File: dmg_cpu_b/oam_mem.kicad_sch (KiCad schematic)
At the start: 27 parts

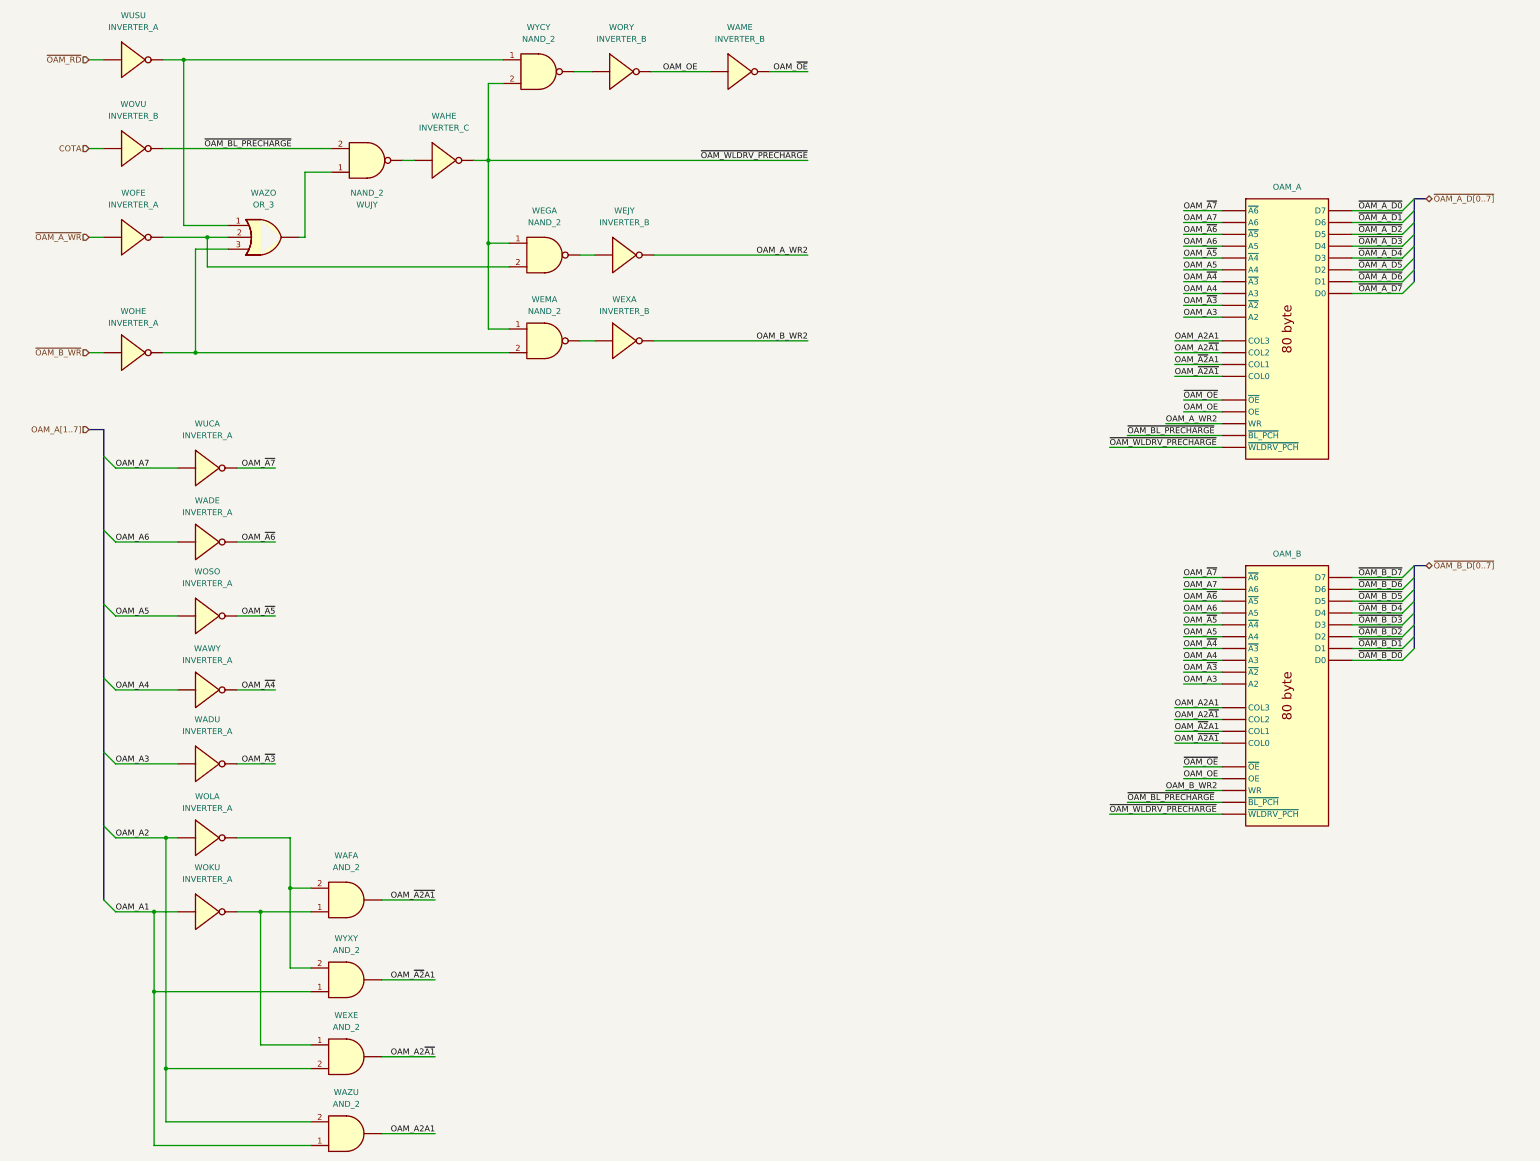
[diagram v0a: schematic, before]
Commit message: Give more meaningful names to cell types
Before this commit, many of the cells types in the chip were named in a
sloppy manner. The different inverter, latch and flip flop valiants were
just suffixed with A, B, C, D, ... Those suffixes gave no information
about the actual differences. They had to be looked up in the
documentation. Now the names of cell types with different variants have
changed:

* Inverter types are named NOT_X1, NOT_X2, NOT_X3, ... The _Xn suffix
  reflects the drive strength of the cell. X1 is the drive strength of
  the weakest inverter, X2 is double the drive strength of the weakest
  inverter.
* Flip flop types are named DFFR, DFFR_CC, DFFR_CC_Q. DFFR is a normal
  data flip flop with reset and a single clock input. The suffix _CC is
  added to flip flops that have two complementary clock inputs (CLK and
  /CLK). Flip flops that only have the positive Q output are suffixed
  with _Q.
* Latch types are named similar to flip flops: DLATCH, DLATCH_EE,
  DLATCH_EE_Q. The suffix _EE is given to latches that require
  "externally inverted enable" signals (ENA and /ENA).
* I/O pad types all start with PAD_BIDIR, PAD_IN or PAD_OUT. They also
  have suffixes that describe what makes them unique, like _PU for
  pull-ups.

Other minor changes were made to align the names with common naming
schemes of other cell libraries.
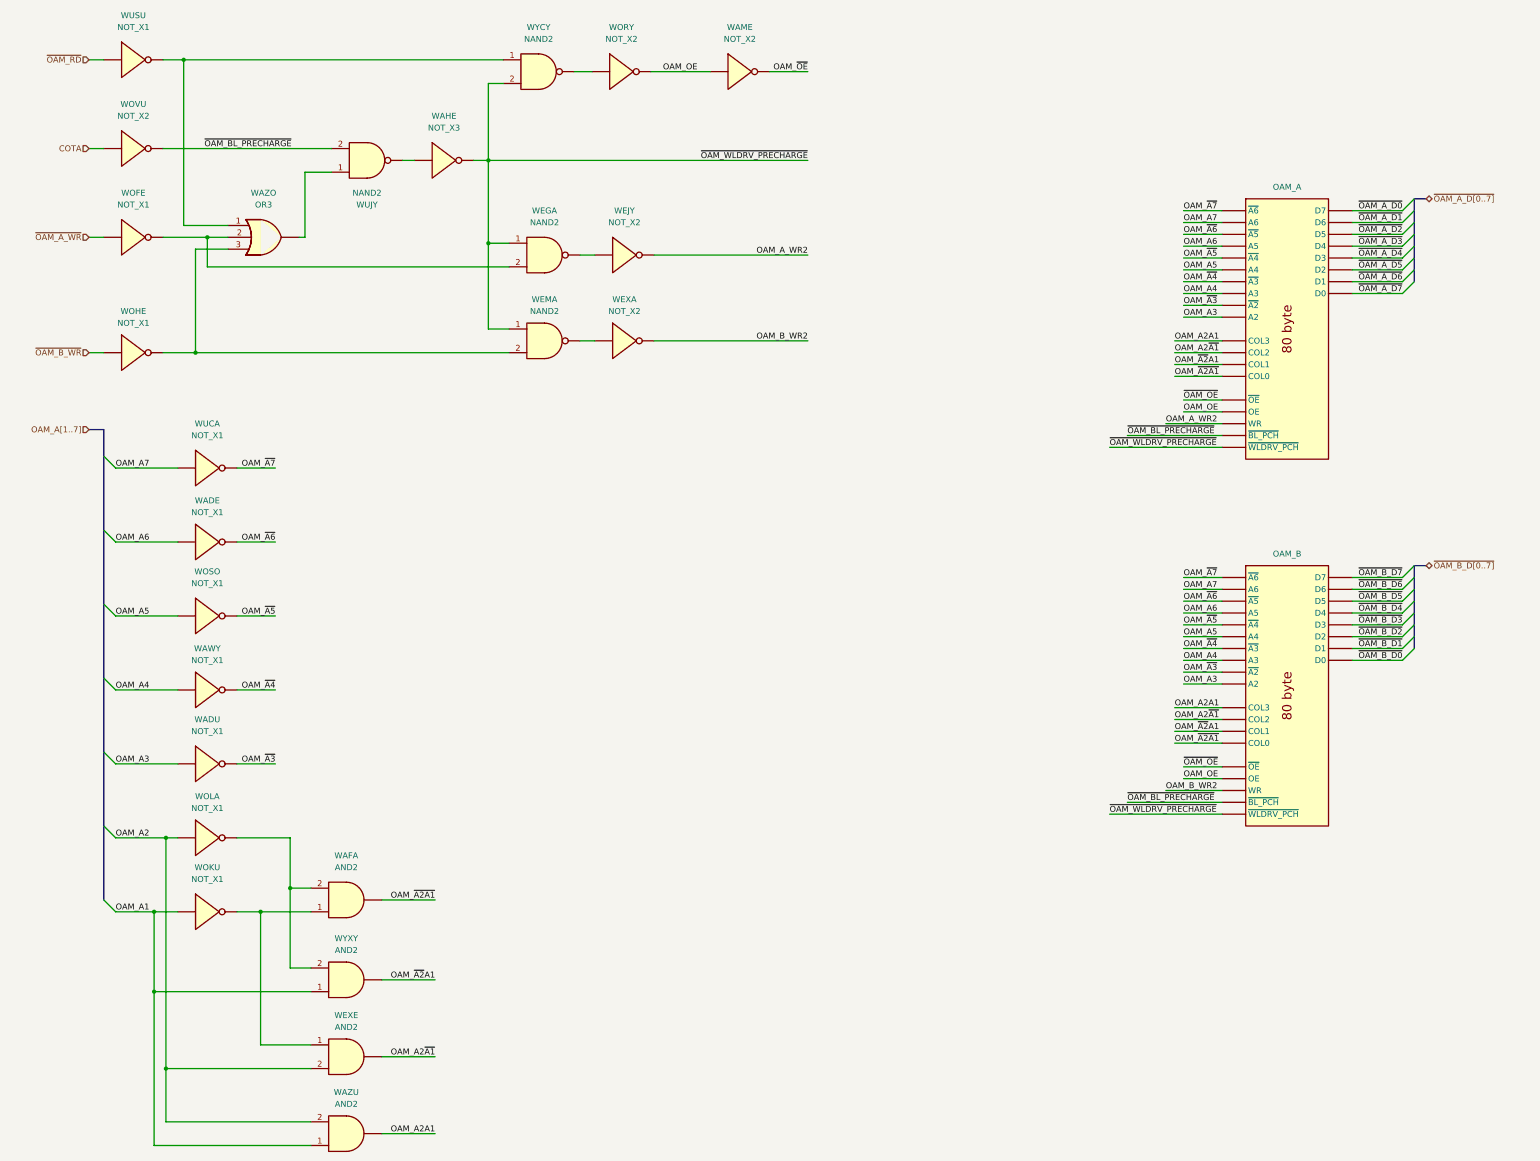
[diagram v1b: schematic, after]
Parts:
- WADE, WADU, WAWY, WOFE, WOHE, WOKU, WOLA, WOSO, WUCA, WUSU: value INVERTER_A -> NOT_X1; symbol DMG_CPU_Cells:INVERTER_A -> DMG_CPU_Cells:NOT_X1
- WAFA, WAZU, WEXE, WYXY: value AND_2 -> AND2; symbol DMG_CPU_Cells:AND_2 -> DMG_CPU_Cells:AND2
- WAHE: value INVERTER_C -> NOT_X3; symbol DMG_CPU_Cells:INVERTER_C -> DMG_CPU_Cells:NOT_X3
- WAME, WEJY, WEXA, WORY, WOVU: value INVERTER_B -> NOT_X2; symbol DMG_CPU_Cells:INVERTER_B -> DMG_CPU_Cells:NOT_X2
- WAZO: value OR_3 -> OR3; symbol DMG_CPU_Cells:OR_3 -> DMG_CPU_Cells:OR3
- WEGA, WEMA, WUJY, WYCY: value NAND_2 -> NAND2; symbol DMG_CPU_Cells:NAND_2 -> DMG_CPU_Cells:NAND2

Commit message: SM83 Layout: Add bottom part of sequencer cells
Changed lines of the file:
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@@
 (kicad_sch
-	(version 20231120)
+	(version 20250114)
 	(generator "eeschema")
-	(generator_version "8.0")
+	(generator_version "9.0")
 	(paper "A3")
 	(title_block
 		(title "DMG-CPU B")
-		(date "2025-04-12")
+		(date "2025-04-22")
 		(rev "0.7")
 		(company "CC-BY-SA-4.0 Régis Galland & Michael Singer -- Derived work from Furrtek")
